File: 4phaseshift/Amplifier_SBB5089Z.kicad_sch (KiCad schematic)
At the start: 6 parts, among them U8 SBB5089Z

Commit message: gerbers generated for 4 element
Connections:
- net VCC renamed LocalVCC
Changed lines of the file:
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@@
+		)
+	)
+	(hierarchical_label "LocalVCC"
+		(shape input)
+		(at 105.41 52.07 90)
+		(effects
+			(font
+				(size 1.27 1.27)
+			)
+			(justify left)
 		)
 	)
@@
 					(unit 1)
 				)
-			)
-		)
-	)
-	(symbol
-		(lib_id "power:VDD")
-		(at 105.41 52.07 0)
-		(mirror y)
-		(unit 1)
-		(exclude_from_sim no)
-		(in_bom yes)
-		(on_board yes)
-		(dnp no)
-		(fields_autoplaced yes)
-		(property "Reference" "#PWR031"
-			(at 105.41 55.88 0)
-			(effects
-				(font
-					(size 1.27 1.27)
-				)
-				(hide yes)
-			)
-		)
-		(property "Value" "VCC"
-			(at 105.41 46.99 0)
-			(effects
-				(font
-					(size 1.27 1.27)
-				)
-			)
-		)
-		(property "Footprint" ""
-			(at 105.41 52.07 0)
-			(effects
-				(font
-					(size 1.27 1.27)
-				)
-				(hide yes)
-			)
-		)
-		(property "Datasheet" ""
-			(at 105.41 52.07 0)
-			(effects
-				(font
-					(size 1.27 1.27)
-				)
-				(hide yes)
-			)
-		)
-		(property "Description" "Power symbol creates a global label with name \"VDD\""
-			(at 105.41 52.07 0)
-			(effects
-				(font
-					(size 1.27 1.27)
-				)
-				(hide yes)
-			)
-		)
-		(pin "1"
-		)
-		(instances
-			(project "4phaseshift"
-				(path "/d1cb1e8f-75d5-4349-ba9b-8e5b2b2c8d07/6d1f04f2-296f-4704-a286-2d8472106751"
-					(reference "#PWR036")
-					(unit 1)
-				)
-				(path "/d1cb1e8f-75d5-4349-ba9b-8e5b2b2c8d07/0761c0aa-3b3e-46c8-a98d-e63cbedea3c2/4dede0cc-0119-469c-af66-dbb2b5279564"
-					(reference "#PWR067")
-					(unit 1)
-				)
-				(path "/d1cb1e8f-75d5-4349-ba9b-8e5b2b2c8d07/3ad94b1c-09d6-4af4-bf9a-a8e5307255e0/4dede0cc-0119-469c-af66-dbb2b5279564"
-					(reference "#PWR0103")
-					(unit 1)
-				)
-				(path "/d1cb1e8f-75d5-4349-ba9b-8e5b2b2c8d07/770cf7ea-21e5-4e4f-888f-d4df42e95689/4dede0cc-0119-469c-af66-dbb2b5279564"
-					(reference "#PWR085")
-					(unit 1)
-				)
-				(path "/d1cb1e8f-75d5-4349-ba9b-8e5b2b2c8d07/d2ba059c-4ec6-43a6-92f4-6c94c9dde8dd/4dede0cc-0119-469c-af66-dbb2b5279564"
-					(reference "#PWR031")
-					(unit 1)
-				)

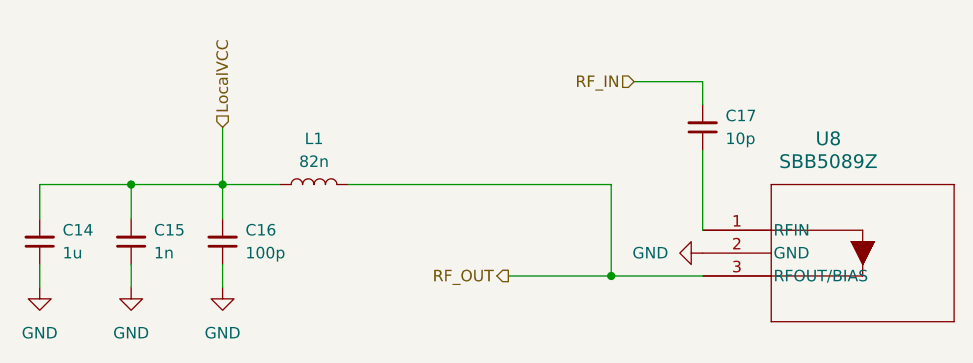
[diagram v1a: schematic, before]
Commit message: updated resistor values
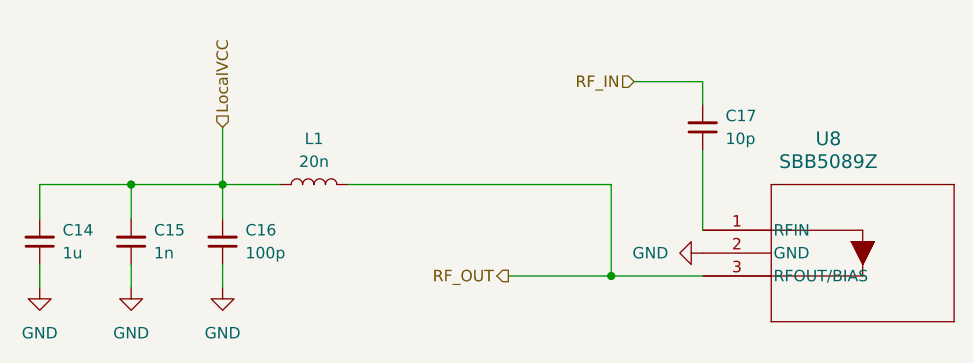
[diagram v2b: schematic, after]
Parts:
- L1: value 82n -> 20n
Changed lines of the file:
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@@
 			)
 		)
-		(property "Value" "82n"
+		(property "Value" "20n"
 			(at 115.57 55.88 90)
 			(effects
